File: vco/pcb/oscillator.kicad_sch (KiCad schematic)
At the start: 58 parts, among them Q2 BC847, U2 TL074, U3 LM13700, U4 ICM7555xB, U5 TL074

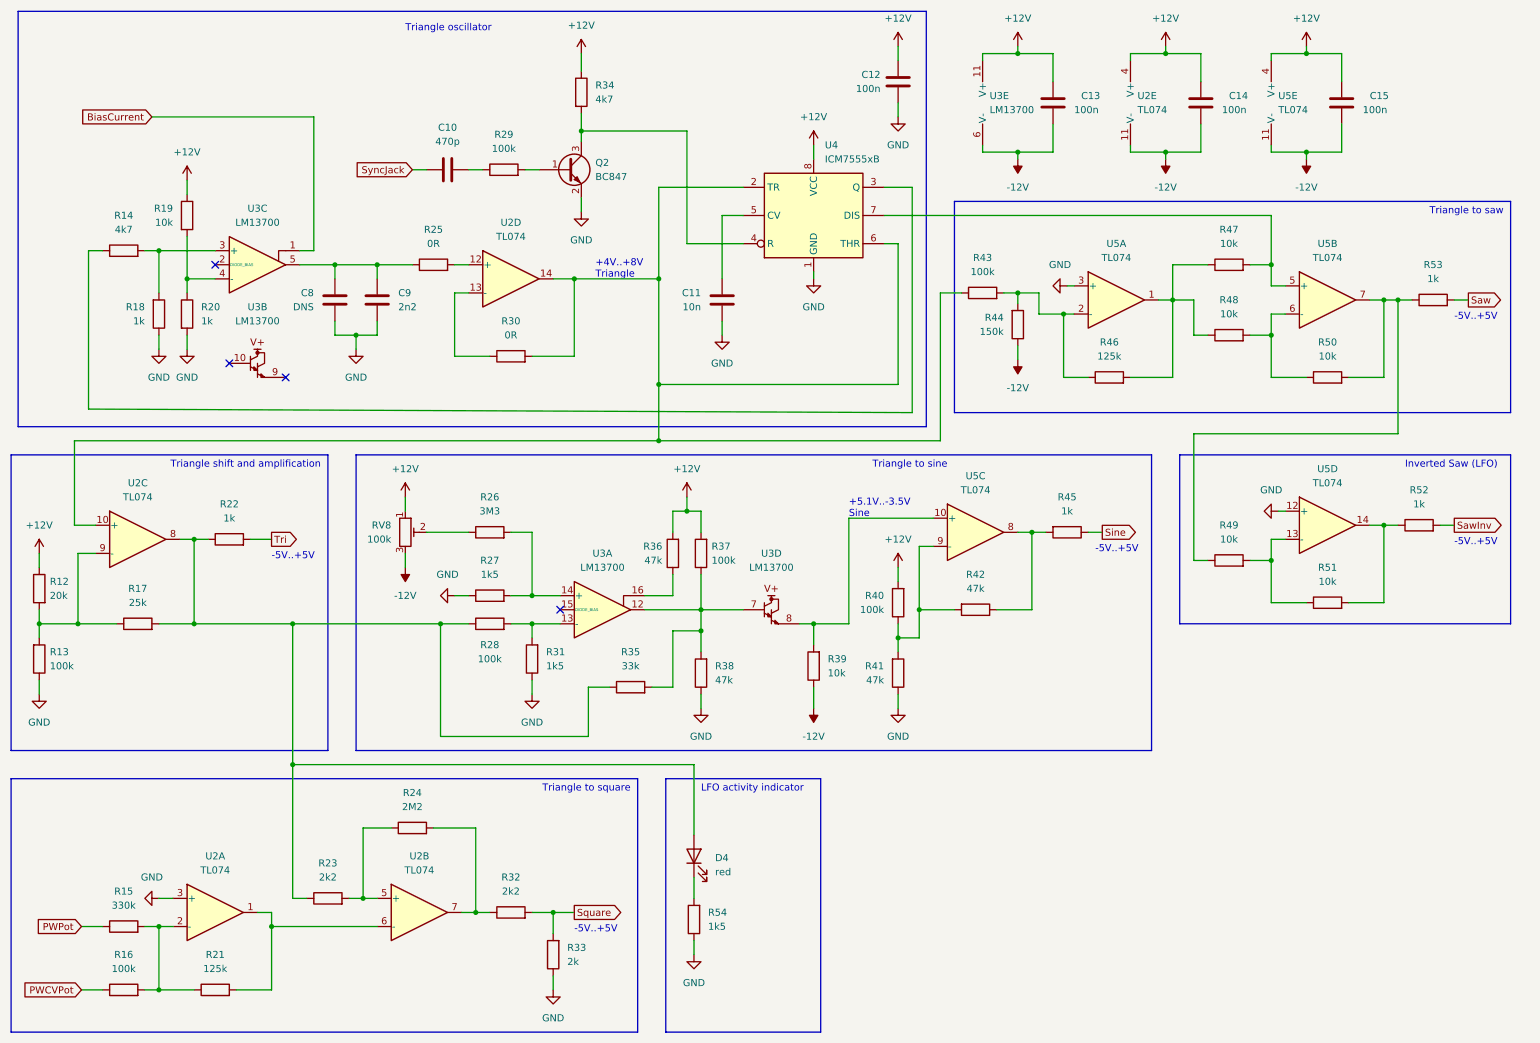
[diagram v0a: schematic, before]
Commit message: vco: Add output dividers for lfo operation
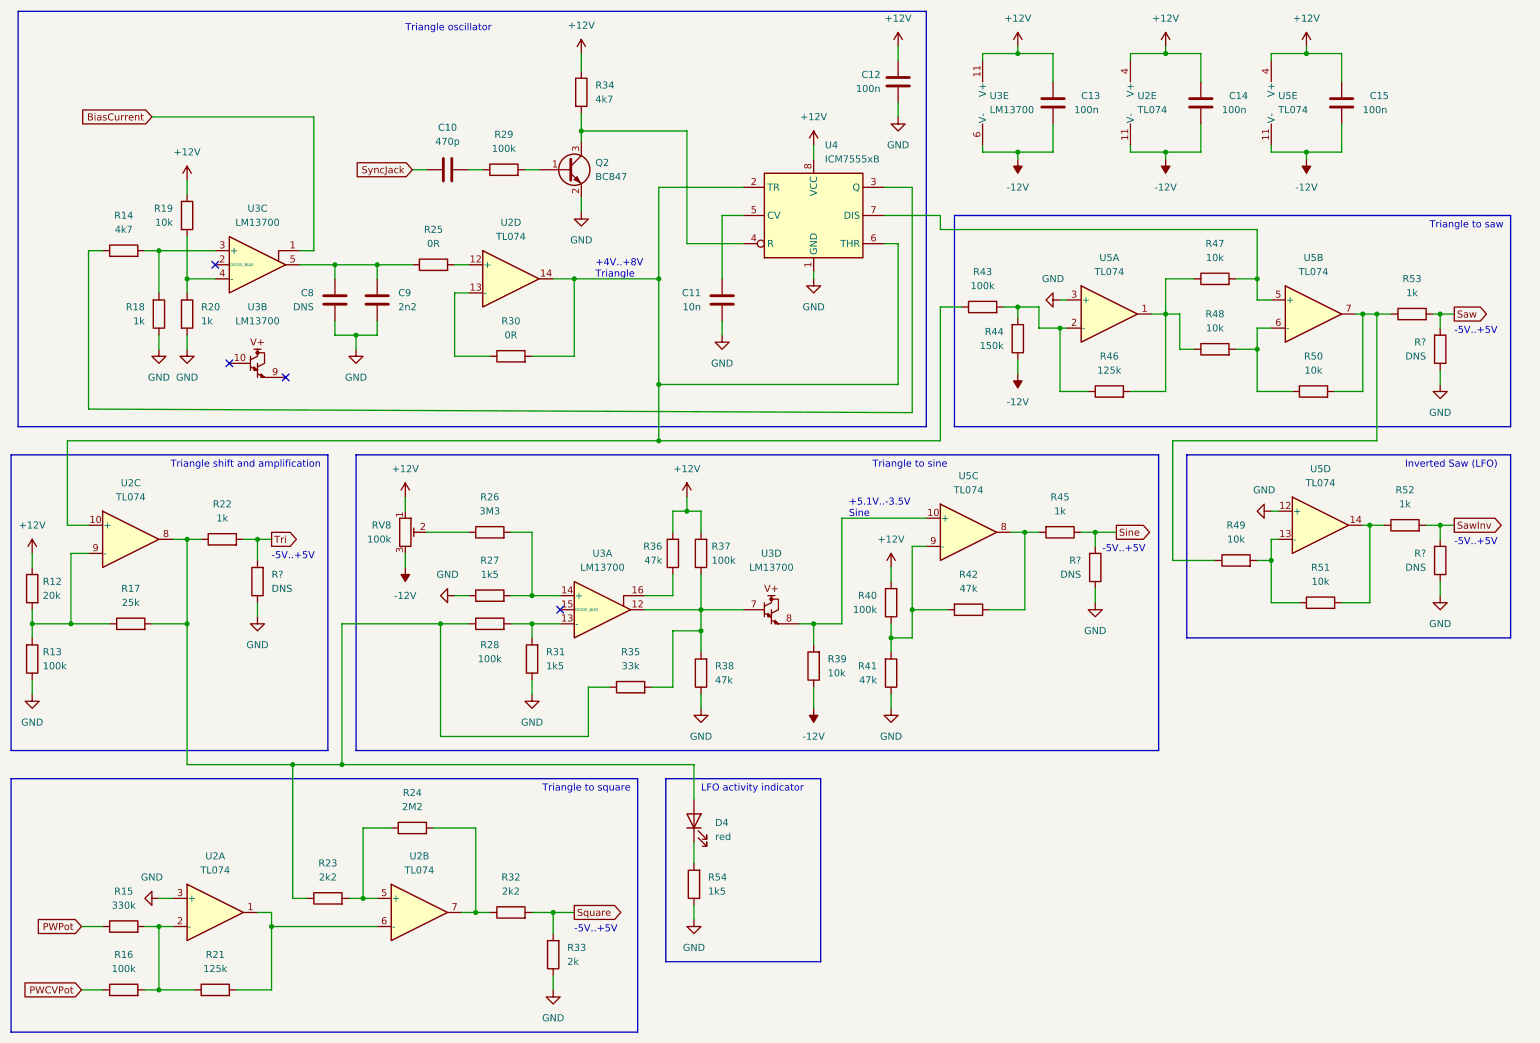
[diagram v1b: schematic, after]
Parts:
- added R? (x4): DNS, Resistor_SMD:R_0603_1608Metric_Pad0.98x0.95mm_HandSolder, symbol Device:R
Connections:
- net GND: now also R?.1, R?.1, R?.1, R?.1
- net Saw: now also R?.2
- net SawInv: now also R?.2
- net Sine: now also R?.2
- net Tri: now also R?.2
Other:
- moved on the sheet: D4, R12, R13, R17, R22, R40, R41, R42, R43, R44, R45, R46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

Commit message: vco: Add a note about the CV input range
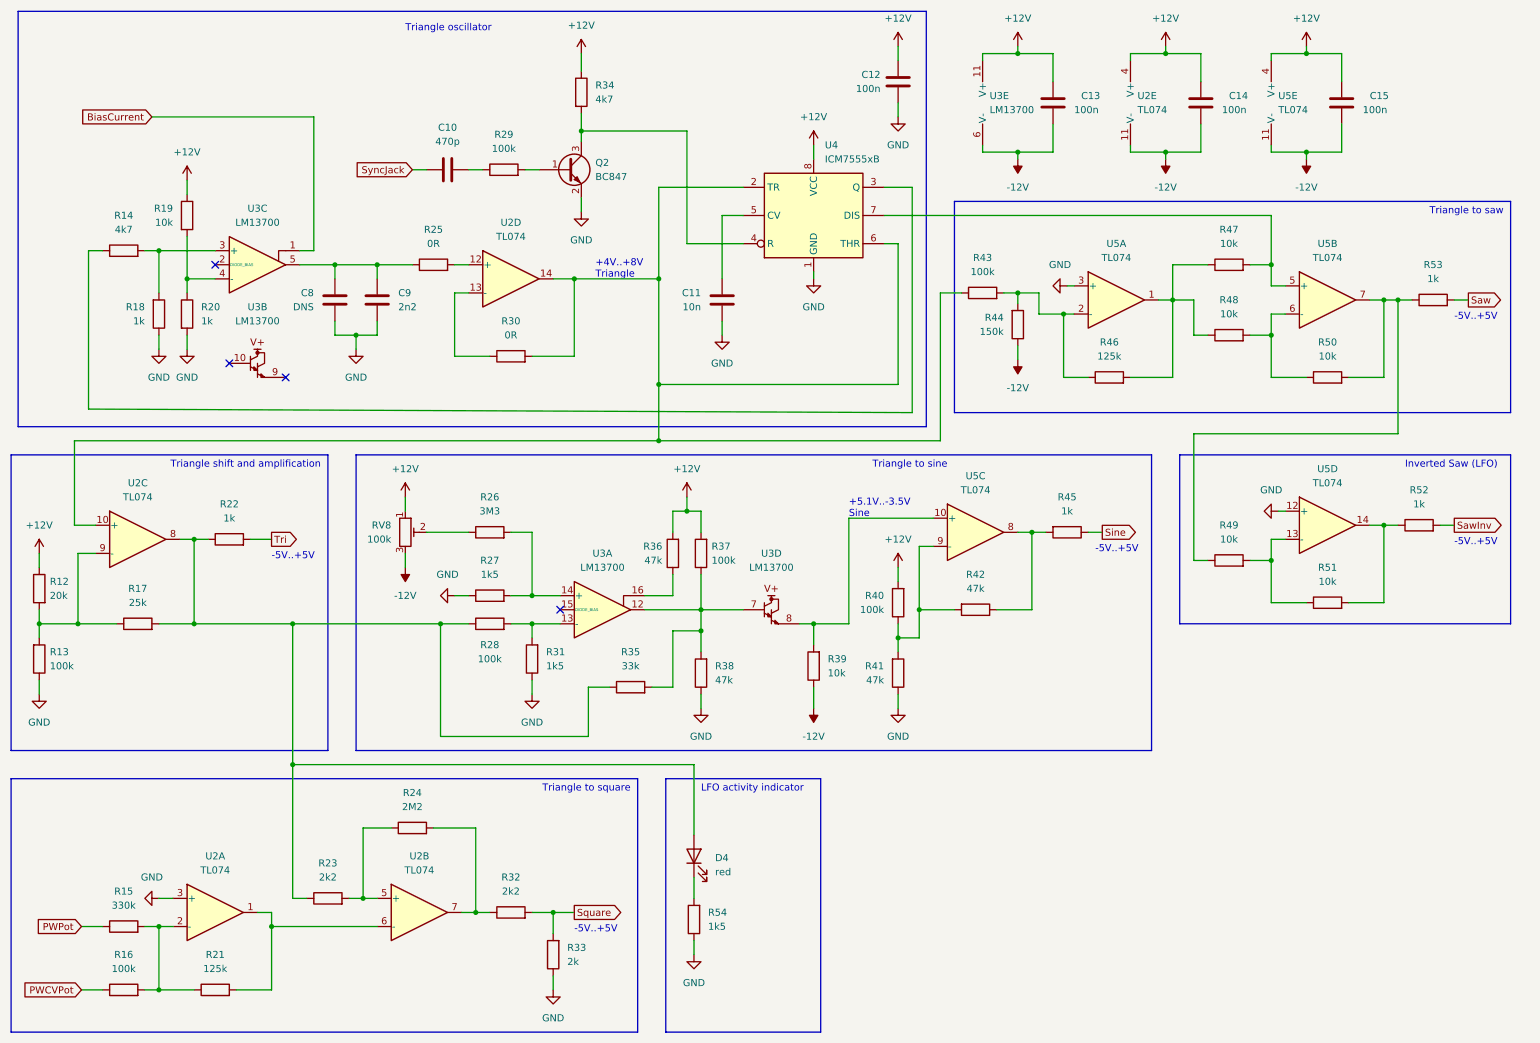
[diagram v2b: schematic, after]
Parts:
- removed R? (x4): DNS, Resistor_SMD:R_0603_1608Metric_Pad0.98x0.95mm_HandSolder, symbol Device:R
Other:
- moved on the sheet: D4, R12, R13, R17, R22, R40, R41, R42, R43, R44, R45, R46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
